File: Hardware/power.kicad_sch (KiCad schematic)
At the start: 65 parts, among them J4 Barrel_Jack_Switch, J8 Conn_01x03, U1 STM32MP157FAD1, U4 STPMIC1

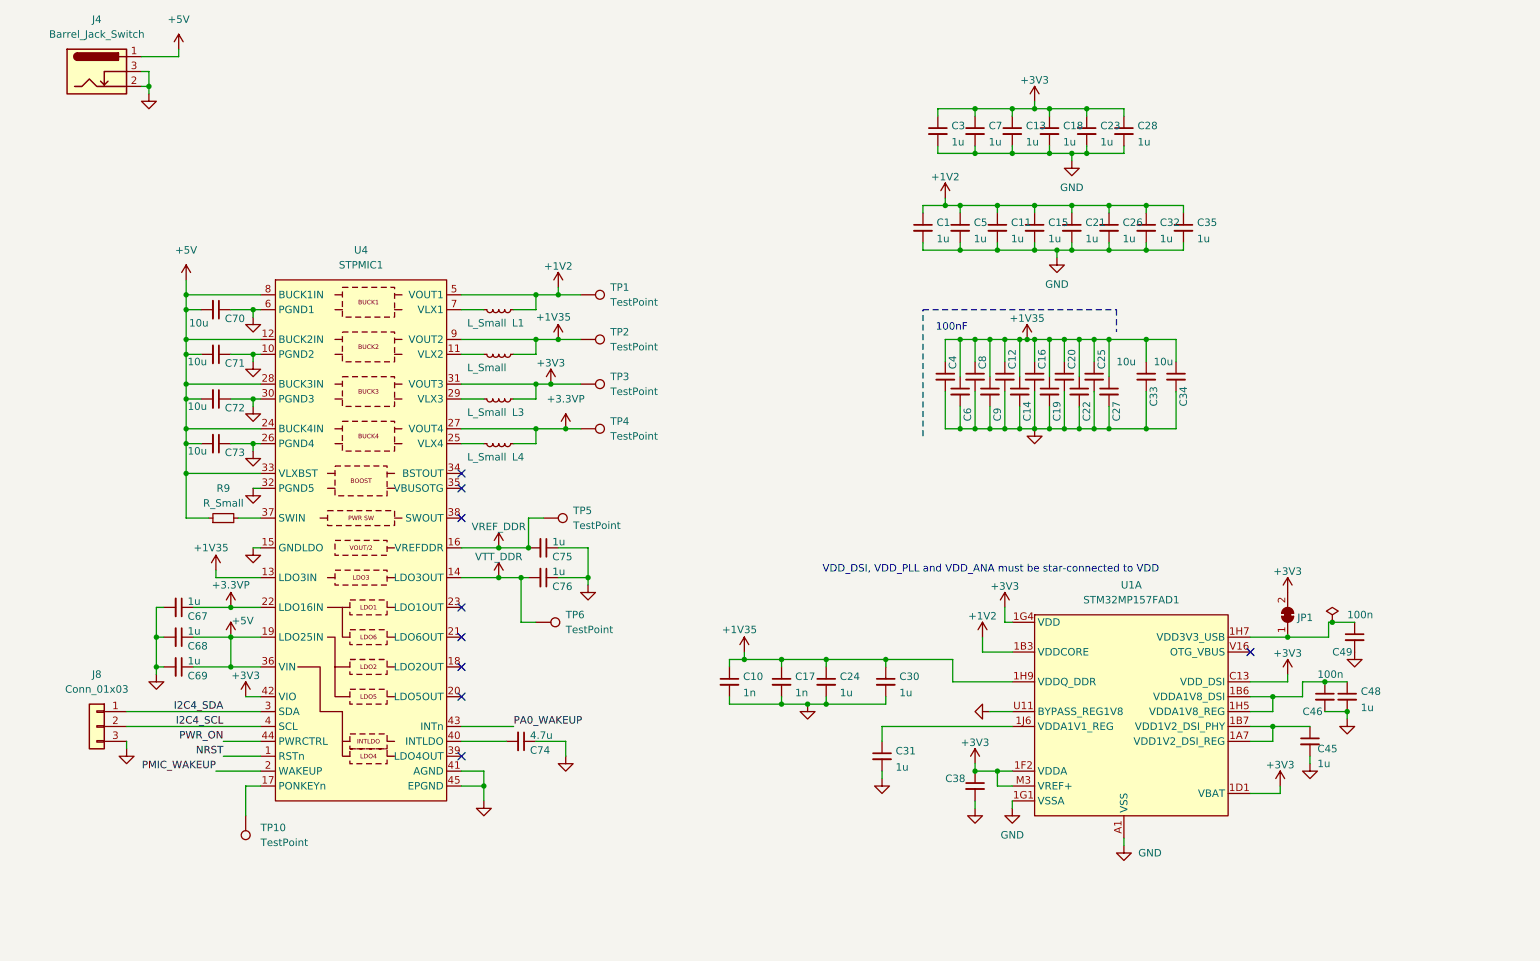
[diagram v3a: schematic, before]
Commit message: Schematic symbol pin type fixes
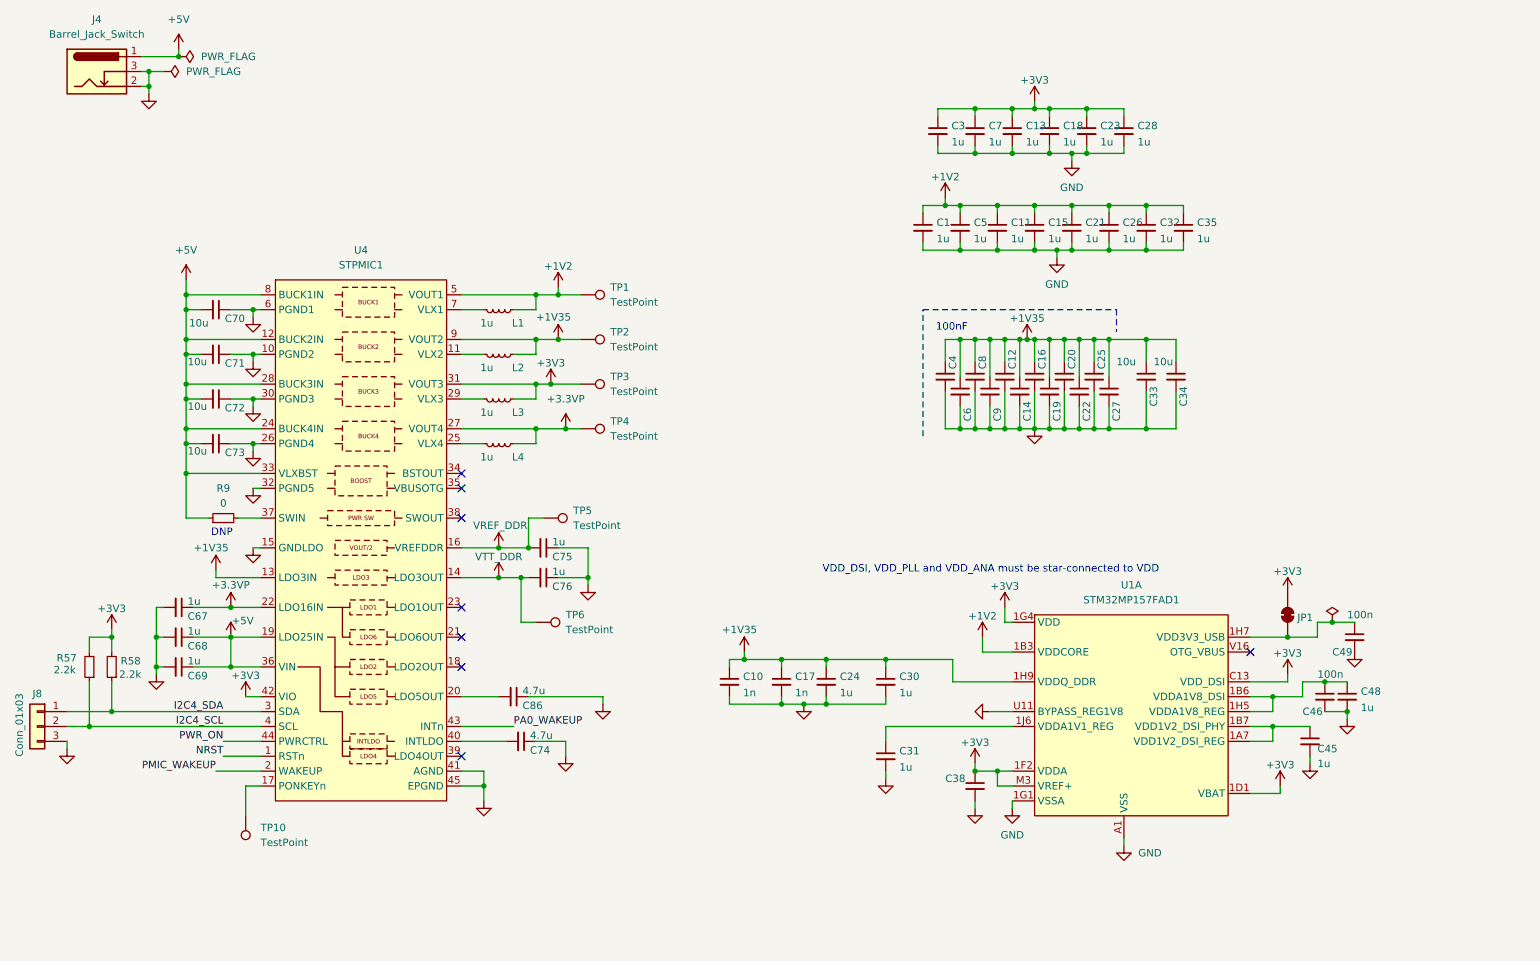
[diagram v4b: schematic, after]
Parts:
- added C86: 4.7u, Capacitor_SMD:C_0402_1005Metric, symbol Device:C_Small
- added R57, R58: 2.2k, Resistor_SMD:R_0402_1005Metric, symbol Device:R_Small
- J4: footprint (none) -> Connector_BarrelJack:BarrelJack_Wuerth_6941xx301002
- J8: footprint (none) -> Connector_PinHeader_2.54mm:PinHeader_1x03_P2.54mm_Vertical
- L1, L2, L3, L4: value L_Small -> 1u; footprint (none) -> Inductor_SMD:L_1008_2520Metric
- R9: value R_Small -> 0; footprint (none) -> Resistor_SMD:R_0402_1005Metric
- TP1, TP10, TP2, TP3, TP4, TP5, TP6: footprint (none) -> TestPoint:TestPoint_Pad_D1.0mm
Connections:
- net +3V3: now also R57.2, R58.2
- net GND: now also C86.1
- net I2C4_SCL: now also R57.1
- net I2C4_SDA: now also R58.1
- net at U4.20 (LDO5OUT): now also C86.2
- no-connect marks 9 -> 8
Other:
- note added: "DNP"
- moved on the sheet: C31, J8

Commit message: First pass through ST Design Checklist
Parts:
- removed C45: 1u, Capacitor_SMD:C_0402_1005Metric, symbol Device:C_Small
- removed JP1: SolderJumper_2_Bridged, Jumper:SolderJumper-2_P1.3mm_Bridged2Bar_Pad1.0x1.5mm, symbol Jumper:SolderJumper_2_Bridged
- added C87, C89, C94: 10u, Capacitor_SMD:C_0603_1608Metric, symbol Device:C_Small
- added C88, C95, C96: 4.7u, Capacitor_SMD:C_0402_1005Metric, symbol Device:C_Small
- added C90, C91, C92, C93: 22u, Capacitor_SMD:C_0805_2012Metric, symbol Device:C_Small
- added R59: 0, Resistor_SMD:R_0402_1005Metric, symbol Device:R_Small
- C69, C76: value 1u -> 4.7u
- C70, C71, C72, C73: footprint Capacitor_SMD:C_0402_1005Metric -> Capacitor_SMD:C_0603_1608Metric
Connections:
- net +1V2: now also C90.2
- net +1V35: now also C87.1, C91.2
- net +3.3VP: now also C93.2
- net +3V3: now also C92.2
- net +5V: now also C89.1, R59.1; no longer U4.33 (VLXBST)
- net GND: now also C87.2, C88.2, C89.2, C90.1, C91.1, C92.1, C93.1, C94.1, C95.1, C96.1
- net VTT_DDR: now also C94.2; no longer C76.2
- net VDD_USB: now reaches C49.1, U1.1H7 (VDD3V3_USB)
- net VDD_USB: now also U4.39 (LDO4OUT), C88.1
- net at U1.1A7 (VDD1V2_DSI_REG): no longer U1.1B7 (VDD1V2_DSI_PHY)
- net at U4.18 (LDO2OUT): now also C76.2
- net at U4.21 (LDO6OUT): now also C95.2
- net at U4.23 (LDO1OUT): now also C96.2
- net NRST renamed ~{RST}
- new net: R59.2, U4.33 (VLXBST)
- no-connect marks 8 -> 6
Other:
- note added: "3V3"
- note added: "VDD"
- note added: "VDDCORE"
- note added: "VDD_DDR"
- moved on the sheet: C74, TP1, TP2, TP3, TP4

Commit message: First Pass Routing
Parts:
- removed R59, R9: 0, Resistor_SMD:R_0402_1005Metric, symbol Device:R_Small
- added C98: 22u, Capacitor_SMD:C_0805_2012Metric, symbol Device:C_Small
- added C99: 4.7u, Capacitor_SMD:C_0402_1005Metric, symbol Device:C_Small
- added JP4, JP5: SolderJumper_3_Bridged12, Jumper:SolderJumper-3_P1.3mm_Bridged2Bar12_Pad1.0x1.5mm, symbol Jumper:SolderJumper_3_Bridged12
- added L5: 1u, Inductor_SMD:L_1008_2520Metric, symbol Device:L_Small
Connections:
- net +5V: now also JP4.1 (A), JP5.1 (A), L5.2
- net GND: now also C98.2, C99.1
- net at U4.37 (SWIN): now also JP4.2 (C)
- net at U4.33 (VLXBST): now also L5.1
- net VOUT_BST: now reaches U4.34 (BSTOUT)
- net VOUT_BST: now also C98.1, JP4.3 (B), JP5.3 (B)
- net PMIC_VBUSOTG: now reaches U4.35 (VBUSOTG)
- net PMIC_VBUSOTG: now also C99.2
- net PMIC_SWOUT: now reaches U4.38 (SWOUT)
- new net VBUS: JP5.2 (C)
- no-connect marks 6 -> 3
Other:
- moved on the sheet: C89, TP5

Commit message: ERC/DRC Clean
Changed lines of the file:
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@@
 		)
 	)
-	(text "DNP"
-		(exclude_from_sim no)
-		(at 50.546 107.95 0)
-		(effects
-			(font
-				(size 1.27 1.27)
-			)
-		)
-	)
 	(text "100nF"
 		(exclude_from_sim no)
@@
 		)
 	)
-	(text "DNP"
-		(exclude_from_sim no)
-		(at 48.26 100.076 0)
-		(effects
-			(font
-				(size 1.27 1.27)
-			)
-		)
-	)
 	(text "VDD_DSI, VDD_PLL and VDD_ANA must be star-connected to VDD"
 		(exclude_from_sim no)
@@
 	)
 	(junction
+		(at 138.43 102.87)
+		(diameter 0)
+		(color 0 0 0 0)
+	)
+	(junction
 		(at 38.1 31.75)
 		(diameter 0)
@@
 	(wire
 		(pts
-			(xy 138.43 105.41) (xy 138.43 106.68)
+			(xy 138.43 101.6) (xy 138.43 102.87)
 		)
 		(stroke
@@
 	(wire
 		(pts
+			(xy 138.43 102.87) (xy 138.43 106.68)
+		)
+		(stroke
+			(width 0)
+			(type default)
+		)
+	)
+	(wire
+		(pts
 			(xy 39.37 105.41) (xy 39.37 106.68)
 		)
@@
 	)
 	(symbol
+		(lib_id "power:PWR_FLAG")
+		(at 138.43 102.87 270)
+		(unit 1)
+		(exclude_from_sim no)
+		(in_bom yes)
+		(on_board yes)
+		(dnp no)
+		(fields_autoplaced yes)
+		(property "Reference" "#FLG02"
+			(at 140.335 102.87 0)
+			(effects
+				(font
+					(size 1.27 1.27)
+				)
+				(hide yes)
+			)
+		)
+		(property "Value" "PWR_FLAG"
+			(at 142.24 102.8699 90)
+			(effects
+				(font
+					(size 1.27 1.27)
+				)
+				(justify left)
+			)
+		)
+		(property "Footprint" ""
+			(at 138.43 102.87 0)
+			(effects
+				(font
+					(size 1.27 1.27)
+				)
+				(hide yes)
+			)
+		)
+		(property "Datasheet" "~"
+			(at 138.43 102.87 0)
+			(effects
+				(font
+					(size 1.27 1.27)
+				)
+				(hide yes)
+			)
+		)
+		(property "Description" "Special symbol for telling ERC where power comes from"
+			(at 138.43 102.87 0)
+			(effects
+				(font
+					(size 1.27 1.27)
+				)
+				(hide yes)
+			)
+		)
+		(pin "1"
+		)
+		(instances
+			(project ""
+				(path "/78ab8a62-95bb-407d-9a77-e3716c9faf5c/64c924ff-1ee2-4076-8d5b-d4197d44b396"
+					(reference "#FLG02")
+					(unit 1)
+				)
+			)
+		)
+	)
+	(symbol
 		(lib_id "power:GND")
 		(at 185.42 154.94 0)
@@
 	(symbol
 		(lib_id "power:VBUS")
-		(at 138.43 105.41 0)
+		(at 138.43 101.6 0)
 		(unit 1)
 		(exclude_from_sim no)
@@
 		(fields_autoplaced yes)
 		(property "Reference" "#PWR0124"
-			(at 138.43 109.22 0)
+			(at 138.43 105.41 0)
 			(effects
 				(font
@@
 		)
 		(property "Value" "VBUS"
-			(at 138.43 100.33 0)
+			(at 138.43 96.52 0)
 			(effects
 				(font
@@
 		)
 		(property "Footprint" ""
-			(at 138.43 105.41 0)
+			(at 138.43 101.6 0)
 			(effects
 				(font
@@
 		)
 		(property "Datasheet" ""
-			(at 138.43 105.41 0)
+			(at 138.43 101.6 0)
 			(effects
 				(font
@@
 		)
 		(property "Description" "Power symbol creates a global label with name \"VBUS\""
-			(at 138.43 105.41 0)
+			(at 138.43 101.6 0)
 			(effects
 				(font

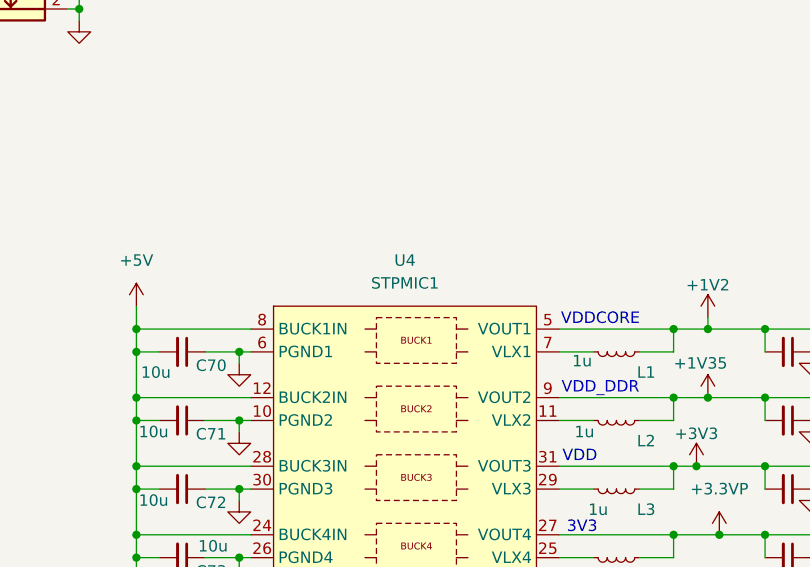
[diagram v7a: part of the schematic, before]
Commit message: Add USB enable pulldowns
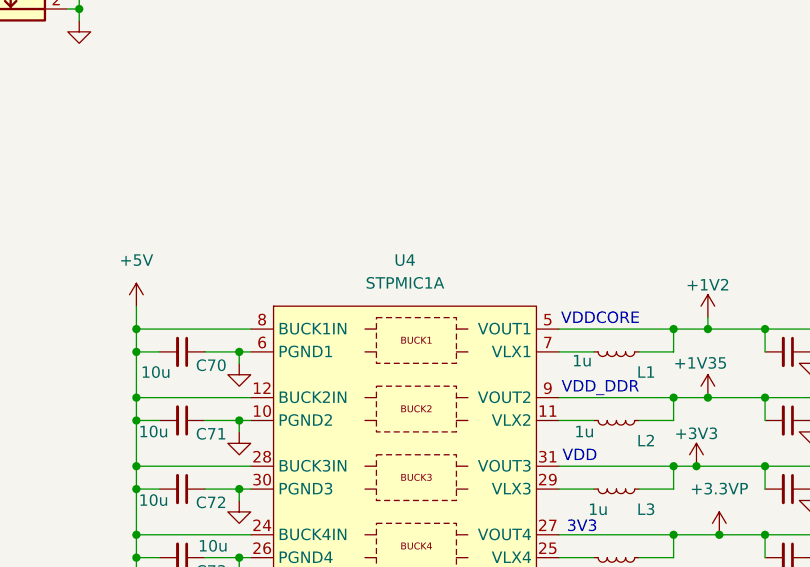
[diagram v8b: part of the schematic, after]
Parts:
- U4: value STPMIC1 -> STPMIC1A
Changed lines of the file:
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@@
 			)
 		)
-		(property "Value" "STPMIC1"
+		(property "Value" "STPMIC1A"
 			(at 74.295 62.23 0)
 			(effects
